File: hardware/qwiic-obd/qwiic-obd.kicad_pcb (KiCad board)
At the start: 4 copper layers, 109.9 x 52.7 mm, 165 parts, among them J101 I2C_STANDARD, J102 DB15_Female_HighDensity, J103 I2C_STANDARD, J401 1x4, J601 PIC ICSP, J602 PIC UART, Q201 2N7002, Q202 2N7002, Q203 2N7002, Q301 2N7002, Q501 DMG2301L, Q502 DMG2301L, Q503 MMBT3906, Q504 DMG2301L, Q601 DMG2301L, Q602 2N7002, Q603 2N7002, Q604 2N7002, Q605 2N7002, Q606 2N7002, Q607 2N7002, Q608 2N7002, Q609 2N7002, Q701 2N7002, Q702 2N7002, Q703 2N7002, Q704 MMBT3904, SW401 SW_Push, SW402 SW_Push, U201 TS5A3359DCUR, U202 TS5A3359DCUR, U203 TS5A3359DCUR, U204 TS5A3359DCUR, U205 TS5A3359DCUR, U301 TH8056KDC-AAA-008-RE, U302 MCP2557FD-xMF, U401 TCA9534, U402 MCP3423, U403 TCA9534, U404 ADM6320BX33ARJZ-R7, U501 AP63203WU, U502 XC9142B50CMR-G, U601 LM317L_SOT-89, U602 NCS20072, U603 PIC16F15225-I/ST, U701 NCS20072, U702 SC16IS741A, U801 SC18IS602BIPW_128, U802 MCP2515-xST, X701 ASV-12.000MHZ-EJ-T, X801 ASV-12.000MHZ-EJ-T

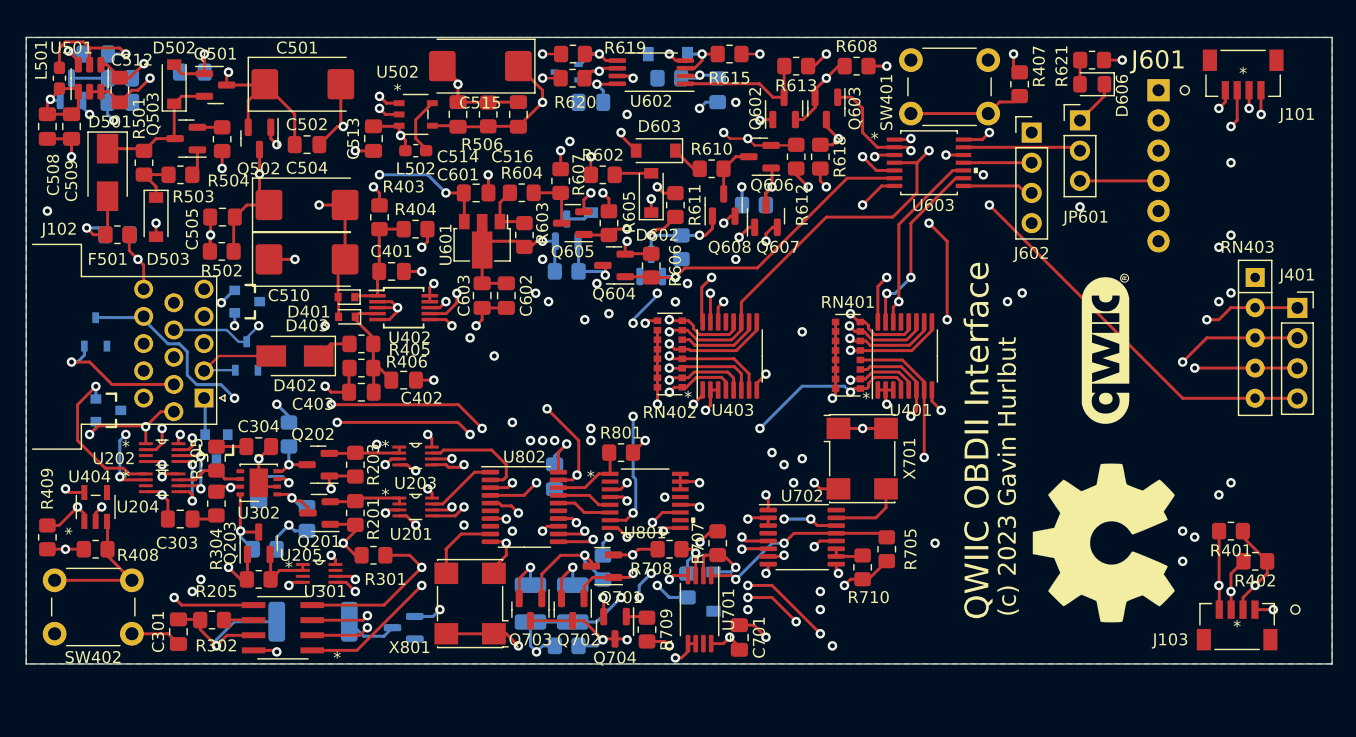
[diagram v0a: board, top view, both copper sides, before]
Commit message: Changed DB15HD connector, fixed layout
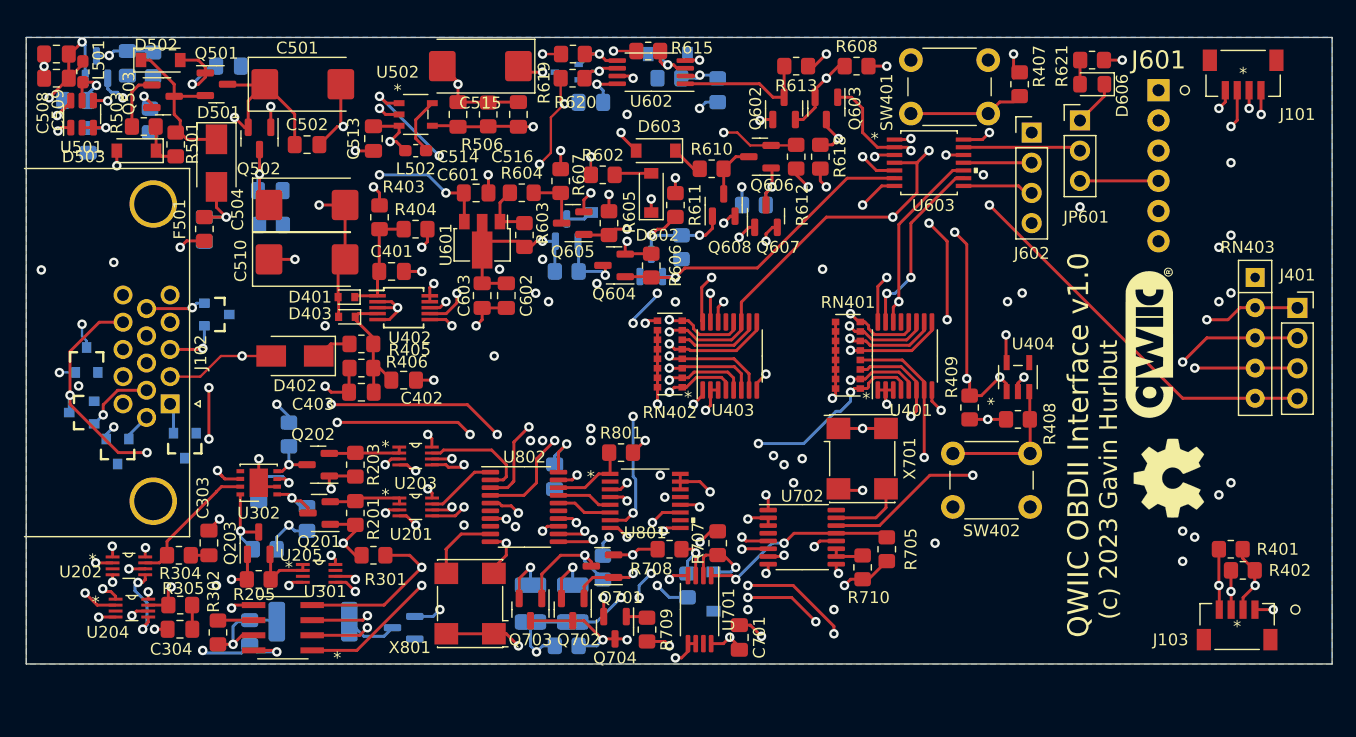
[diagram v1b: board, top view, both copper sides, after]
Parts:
- removed the REF** at (198.6, 114.3)
- added REF**: OSHW-Symbol_6.7x6mm_SilkScreen, Symbol:OSHW-Symbol_6.7x6mm_SilkScreen, F.Cu at (204.1, 108.8)
- C301, C505, C512, R502, R504: moved to B.Cu
- D101, D102: footprint UltraLibrarian:MMBZ27VALT116 -> SparkFun-DiscreteSemi:SOT23-3
- J102: value DB15_Female_HighDensity -> DB15_Female_HighDensity_MountingHoles; footprint Connector_Dsub:DSUB-15-HD_Female_Horizontal_P2.29x2.54mm_EdgePinOffset9.40mm -> Connector_Dsub:DSUB-15-HD_Female_Horizontal_P2.29x1.98mm_EdgePinOffset8.35mm_Housed_MountingHolesOffset10.89mm
- moved R409 78.3 mm to (187.3, 102.9)
- moved R408 78.3 mm to (191.4, 103.9)
- moved U404 78.3 mm to (191.4, 100.3)
- moved SW402 76.3 mm to (192.4, 111.3)
- moved C304 16.7 mm to (120.9, 121.5), turned to 180 degrees
- moved D102 13.5 mm to (113.0, 98.9)
- moved R305 12.7 mm to (120.9, 119.5), turned to 0 degrees
- moved U204 10.8 mm to (116.8, 119.8)
- moved U202 9.93 mm to (116.6, 116.2)
- moved D501 9.19 mm to (124.0, 82.3)
- moved F501 7.33 mm to (122.9, 87.9), turned to -90 degrees
- moved C503 7.33 mm to (122.9, 87.9), turned to 90 degrees
- moved D101 6.88 mm to (112.7, 103.3), turned to -90 degrees
- moved R615 6.85 mm to (160.3, 72.9), turned to 180 degrees
- moved R504 6.26 mm to (118.4, 78.7)
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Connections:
- D104 pad 1: HS_CAN_HI -> HS_CAN_LO
- D104 pad 2: HS_CAN_LO -> HS_CAN_HI
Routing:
- net +3V3_NOSW: track 197.3 -> 154.7 mm, vias 12 -> 14
- net ~{RESET}: track 150.3 -> 126.2 mm, vias 9 -> 10
- net VBAT: track 64.7 -> 87.1 mm
- net L_LINE: track 56.7 -> 70.6 mm, vias 5 -> 6
- net MS_CAN_LO: track 24.7 -> 38.3 mm
- net MS_CAN_HI: track 17.7 -> 30.4 mm, vias 2 -> 4
- net CAN_LO: track 5.82 -> 17.6 mm, vias 0 -> 2
- net GND: track 154.4 -> 144.9 mm, vias 55 -> 56
- net J1850_BUS-: track 87.0 -> 79.6 mm, vias 10 -> 7
- net HS_CAN_LO: track 19.6 -> 26.8 mm, vias 1 -> 2
- net SW_CAN: track 43.7 -> 37.0 mm, vias 1 -> 2
- net Net-(C507-Pad1): track 10.9 -> 4.40 mm
- net J1850_BUS+: track 96.4 -> 90.1 mm
- net HS_CAN_HI: track 10.7 -> 15.4 mm, vias 2 -> 1
- net ~{ISO_TX}: track 26.8 -> 22.4 mm, vias 4 -> 2
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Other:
- board text added: "QWIIC OBDII Interface v1.0"
- board text removed: "QWIIC OBDII Interface"

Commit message: Shrunk layout a bit
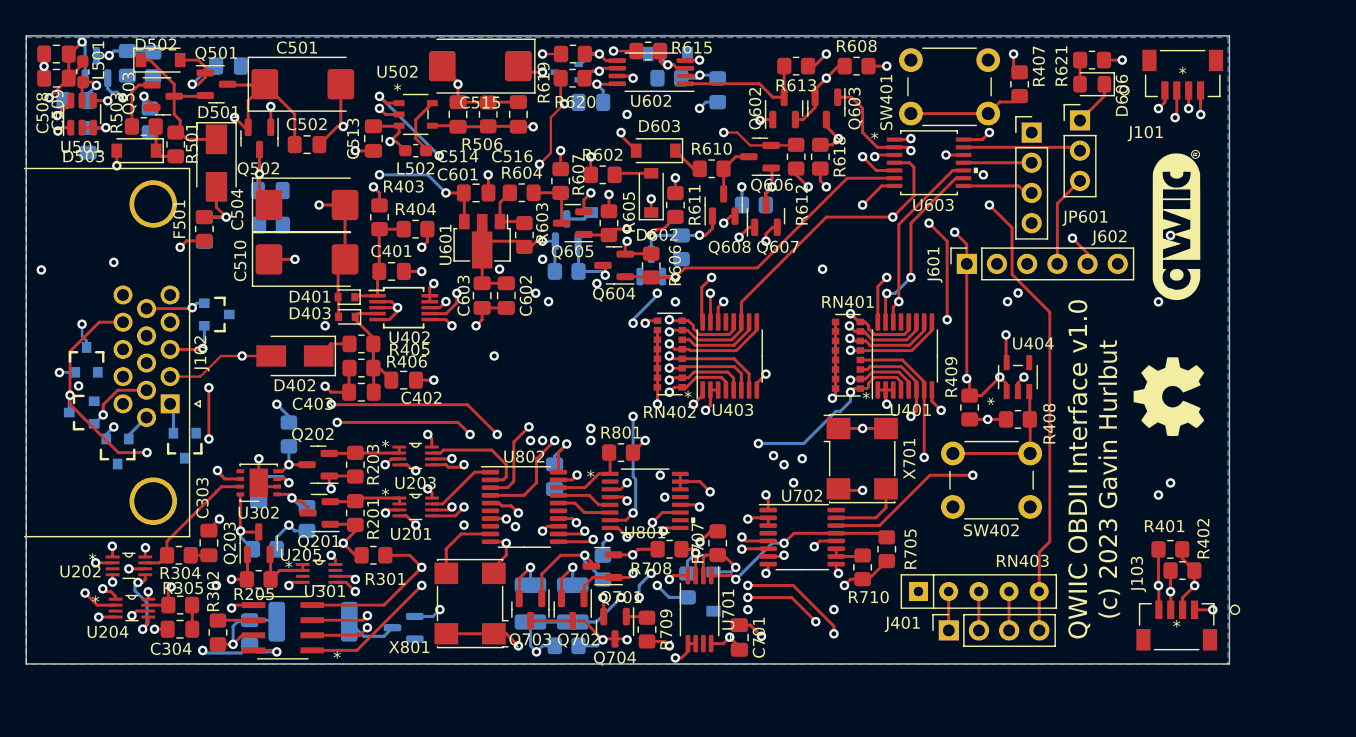
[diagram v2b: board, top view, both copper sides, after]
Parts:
- J601: footprint SparkFun-Connectors:MOLEX-1X6 -> Connector_PinSocket_2.54mm:PinSocket_1x06_P2.54mm_Vertical
- moved J401 40.0 mm to (185.6, 121.6), turned to 90 degrees
- moved RN403 38.7 mm to (183.0, 118.4), turned to 0 degrees
- moved J601 21.8 mm to (187.1, 90.8), turned to 90 degrees
- moved G*** 10.2 mm to (204.6, 87.6)
- moved REF** 6.86 mm to (204.1, 102.0)
- moved J103 5.08 mm to (204.7, 121.3)
- moved J101 5.08 mm to (205.2, 74.8)
- moved R401 5.08 mm to (204.2, 114.8)
- moved R402 5.08 mm to (205.2, 116.6)
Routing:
- net ~{CAN_INT}: track 89.8 -> 42.4 mm, vias 5 -> 3
- net ~{SPI_INT}: track 79.3 -> 41.1 mm, vias 5 -> 3
- net ~{UART_INT}: track 60.5 -> 22.3 mm, vias 4 -> 1
- net ~{RESET}: track 126.2 -> 102.1 mm, vias 10 -> 9
- net +3V3_NOSW: track 154.7 -> 138.5 mm
- net ~{J1850_INT}: track 46.7 -> 52.3 mm
- net SCL: track 166.2 -> 161.1 mm
- net SDA: track 167.1 -> 162.3 mm
- net ICSPCLK: track 21.3 -> 17.7 mm
- net SW_CAN_LOAD: track 66.8 -> 63.9 mm
- net ICSPDAT: track 6.60 -> 7.77 mm
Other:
- board size 109.9 x 52.7 mm -> 101.2 x 52.8 mm

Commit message: Moved to using shared KiCad libs, regen gerbers
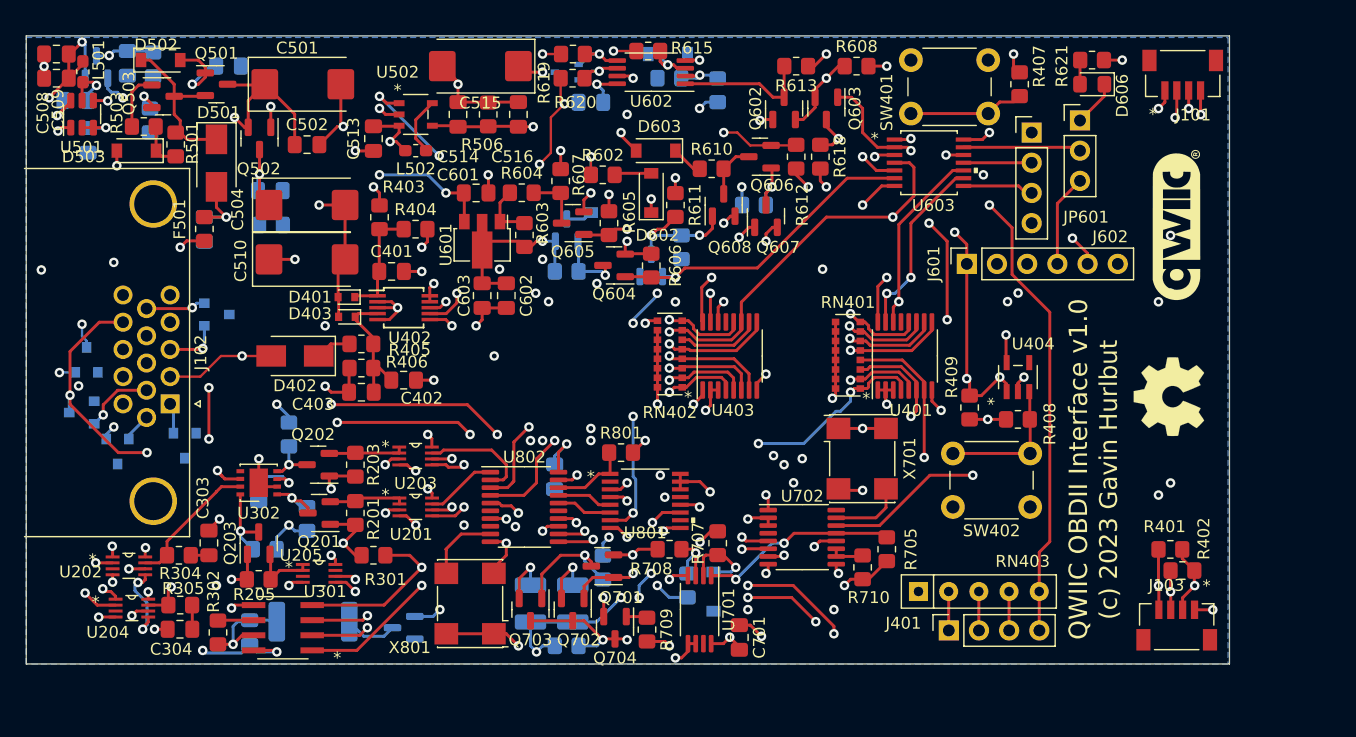
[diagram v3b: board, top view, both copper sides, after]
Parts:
- D101, D102, D103, D104, D105: footprint SparkFun-DiscreteSemi:SOT23-3 -> SparkFun-Silicon-Standard:SOT23-3
- D602, D603: value BAT46W -> BAT46J
- D701: value BAT54W -> BAT54J
- G***: footprint local:qwiic-logo -> Beirdo:qwiic-logo
- J101, J103: value I2C_STANDARD -> QWIIC Connector; footprint UltraLibrarian:PRT-16766 -> Beirdo:QWIIC Connector
- U404: value ADM6320BX33ARJZ-R7 -> APX823-31W5G-7

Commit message: Switch out the PIC for an ATtiny424.
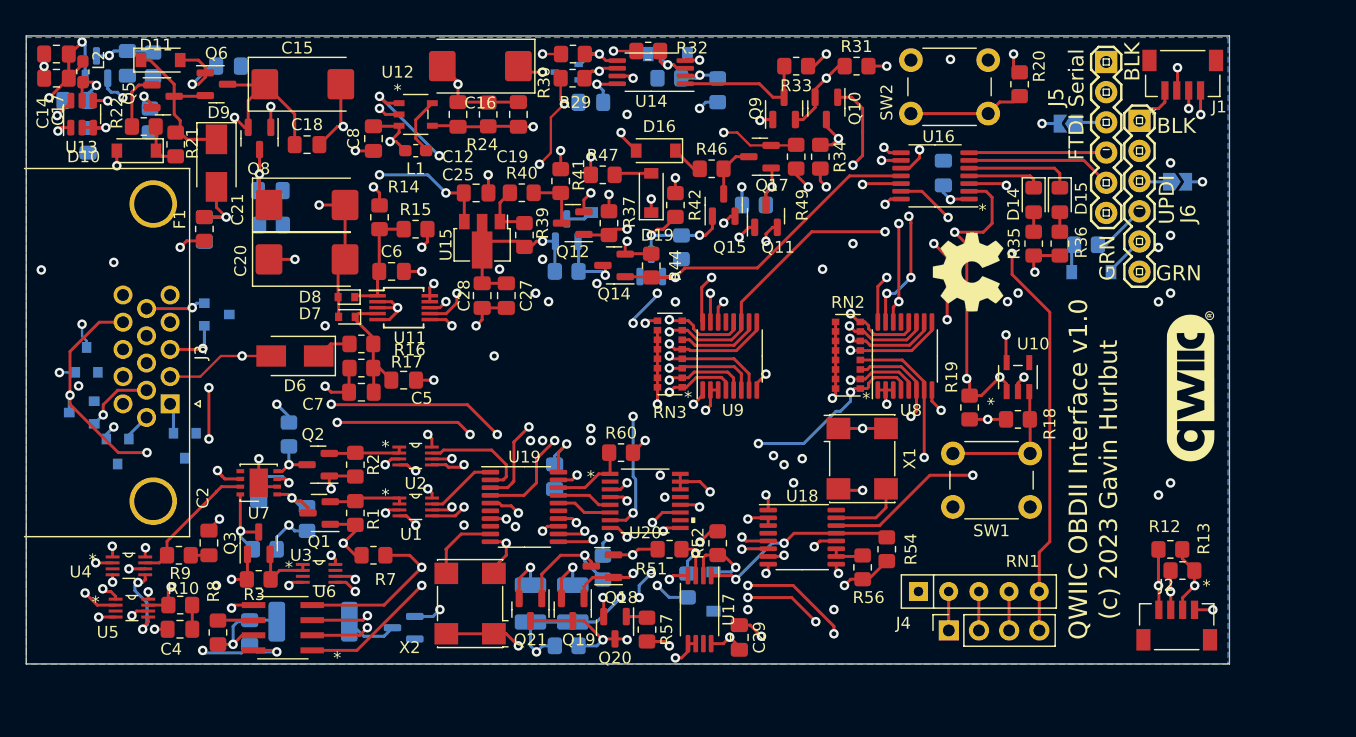
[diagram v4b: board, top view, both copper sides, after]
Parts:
- removed D606: LED, LED_SMD:LED_0805_2012Metric_Pad1.15x1.40mm_HandSolder
- removed J601: PIC ICSP, Connector_PinSocket_2.54mm:PinSocket_1x06_P2.54mm_Vertical
- removed J602: PIC UART, Connector_PinHeader_2.54mm:PinHeader_1x04_P2.54mm_Vertical
- removed JP601: BL_LED = 1,2 ICSP_DAT = 2,3, Connector_PinHeader_2.54mm:PinHeader_1x03_P2.54mm_Vertical
- removed R621: 330, Resistor_SMD:R_0805_2012Metric_Pad1.20x1.40mm_HandSolder
- removed U603: PIC16F15225-I/ST, UltraLibrarian:PIC16F15225-I&slash_ST
- added C26: 100nF, Capacitor_SMD:C_0805_2012Metric_Pad1.18x1.45mm_HandSolder, B.Cu at (185.1, 83.2)
- added D14: LED, LED_SMD:LED_0805_2012Metric_Pad1.15x1.40mm_HandSolder, F.Cu at (192.7, 85.4)
- added D15: LED, LED_SMD:LED_0805_2012Metric_Pad1.15x1.40mm_HandSolder, F.Cu at (194.9, 85.4)
- added D18: BAT42W-V, Diode_SMD:D_SOD-123, B.Cu at (197.6, 91.5)
- added J5: FTDI Serial, Beirdo:FTDI_BASIC, F.Cu at (198.8, 73.8)
- added J6: UPDI, Beirdo:FTDI_BASIC, F.Cu at (201.6, 78.8)
- added JP1: Solder Jumper, Jumper:SolderJumper-2_P1.3mm_Open_TrianglePad1.0x1.5mm, B.Cu at (195.6, 79.0)
- added JP2: Solder Jumper, Jumper:SolderJumper-2_P1.3mm_Open_TrianglePad1.0x1.5mm, B.Cu at (204.8, 83.9)
- added R35: 330R, Resistor_SMD:R_0805_2012Metric_Pad1.20x1.40mm_HandSolder, F.Cu at (192.7, 89.1)
- added R36: 330R, Resistor_SMD:R_0805_2012Metric_Pad1.20x1.40mm_HandSolder, F.Cu at (194.9, 89.1)
- added R48: 470R, Resistor_SMD:R_0805_2012Metric_Pad1.20x1.40mm_HandSolder, B.Cu at (197.1, 89.2)
- added U16: ATtiny424-X, Package_SO:TSSOP-14_4.4x5mm_P0.65mm, F.Cu at (184.4, 83.4)
- moved REF** 19.9 mm to (187.2, 91.5)
- moved G*** 13.6 mm to (205.8, 101.2)
- renumbered C302 to C1, C512 to C10, C507 to C11, C514 to C12, C506 to C13, C508 to C14, C501 to C15, C515 to C16, C509 to C17, C502 to C18, C516 to C19, C303 to C2, C510 to C20, C504 to C21, C511 to C22, C505 to C23, C604 to C24, C601 to C25, C602 to C27, C603 to C28, C701 to C29, C301 to C3, C801 to C30, C304 to C4, C402 to C5, C401 to C6, C403 to C7, C513 to C8, C503 to C9, D105 to D1, D503 to D10, D502 to D11, D605 to D12, D604 to D13, D603 to D16, D601 to D17, D602 to D19, D104 to D2, D701 to D20, D103 to D3, D101 to D4, D102 to D5, D402 to D6, D403 to D7, D401 to D8, D501 to D9, F501 to F1, J101 to J1, J103 to J2, J102 to J3, J401 to J4, L502 to L1, L501 to L2, Q201 to Q1, Q603 to Q10, Q607 to Q11, Q605 to Q12, Q609 to Q13, Q604 to Q14, Q608 to Q15, Q601 to Q16, Q606 to Q17, Q701 to Q18, Q702 to Q19, Q202 to Q2, Q704 to Q20, Q703 to Q21, Q203 to Q3, Q301 to Q4, Q503 to Q5, Q501 to Q6, Q504 to Q7, Q502 to Q8, Q602 to Q9, R201 to R1, R305 to R10, R303 to R11, R401 to R12, R402 to R13, R403 to R14, R404 to R15, R405 to R16, R406 to R17, R408 to R18, R409 to R19, R203 to R2, R407 to R20, R501 to R21, R503 to R22, R504 to R23, R506 to R24, R505 to R25, R502 to R26, R614 to R27, R617 to R28, R620 to R29, R205 to R3, R619 to R30, R608 to R31, R615 to R32, R613 to R33, R618 to R34, R605 to R37, R609 to R38, R603 to R39, R202 to R4, R604 to R40, R607 to R41, R611 to R42, R601 to R43, R606 to R44, R616 to R45, R610 to R46, R602 to R47, R612 to R49, R204 to R5, R704 to R50, R708 to R51, R707 to R52, R701 to R53, R705 to R54, R702 to R55, R710 to R56, R709 to R57, R706 to R58, R703 to R59, R206 to R6, R801 to R60, R301 to R7, R302 to R8, R304 to R9, RN403 to RN1, RN401 to RN2, RN402 to RN3, SW402 to SW1, SW401 to SW2, U201 to U1, U404 to U10, U402 to U11, U502 to U12, U501 to U13, U602 to U14, U601 to U15, U701 to U17, U702 to U18, U802 to U19, U203 to U2, U801 to U20, U205 to U3, U202 to U4, U204 to U5, U301 to U6, U302 to U7, U401 to U8, U403 to U9, X701 to X1, X801 to X2
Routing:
- net UPDI: track 0.00 -> 27.9 mm, vias 0 -> 1
- net ICSPCLK: track 17.7 -> 0.00 mm, vias 3 -> 0
- net AVR_RX: track 0.00 -> 12.3 mm
- net AVR_TX: track 0.00 -> 11.5 mm
- net PA0: track 9.92 -> 0.00 mm
- net SAE_PWM: track 75.4 -> 84.5 mm, vias 6 -> 8
- net ~{J1850_LED}: track 0.00 -> 9.02 mm
- net ICSPDAT: track 7.77 -> 0.00 mm
- net ~{J1850_INT}: track 52.3 -> 44.9 mm
- net ~{PIC_BL_ENTRY}: track 15.6 -> 9.04 mm, vias 1 -> 0
- net ~{AVR_LED}: track 0.00 -> 6.26 mm
- net PIC_TX: track 5.98 -> 0.00 mm
- net PIC_RX: track 5.73 -> 0.00 mm
- net Net-(R48-Pad2): track 0.00 -> 4.67 mm
- net ~{PIC_BL_LED}: track 3.90 -> 0.00 mm
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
